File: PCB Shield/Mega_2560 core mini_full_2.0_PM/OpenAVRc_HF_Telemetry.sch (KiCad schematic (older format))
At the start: 12 parts, among them P18 Ecolage, P19 Module_TX, P20 TTL/RS232, P7 SPIX, U1 74LVC1G3157GV, U2 TLP290, U3 TLP290, U9 4050

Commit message: Delete cd4050 and move BT on board
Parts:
- removed U9: 4050, SO-16-N, symbol 4050-RESCUE-Mega_2560_core_mini_full_2.0
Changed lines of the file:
@@
 	5700 1750 5500 1750
 Connection ~ 5500 1750
-$Comp
-L 4050-RESCUE-Mega_2560_core_mini_full_2.0 U9
-U 1 1 59C530CC
-P 7300 1450
-F 0 "U9" H 7495 1565 60  0000 C CNN
-F 1 "4050" H 7490 1325 60  0000 C CNN
-F 2 "SO-16-N" H 7300 1450 60  0001 C CNN
-F 3 "" H 7300 1450 60  0001 C CNN
-	1    7300 1450
-	1    0    0    -1
-$EndComp
 Wire Notes Line
 	6250 4850 10250 4850

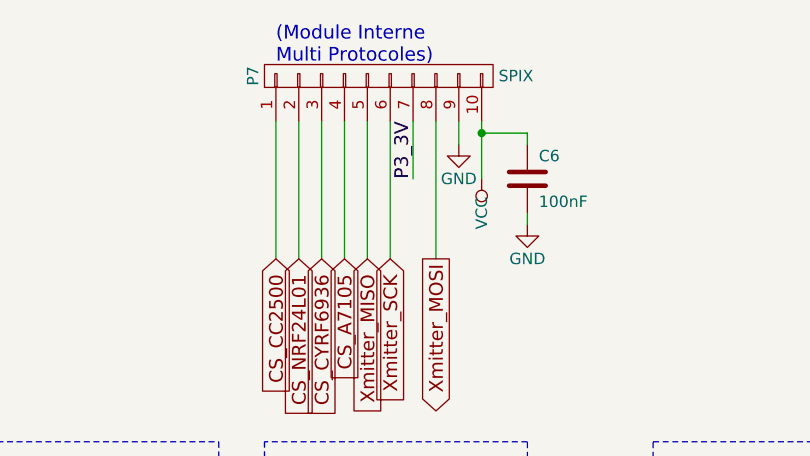
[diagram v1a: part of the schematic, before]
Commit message: Replace P3_3V signal by +3,3V (solve no connected plane on top)
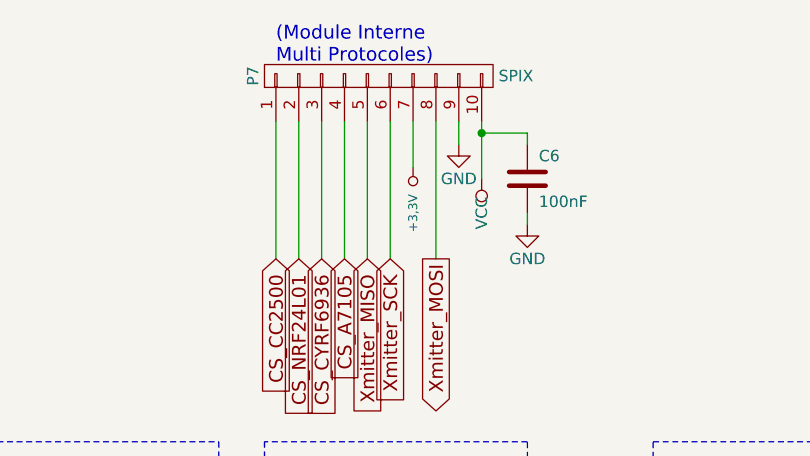
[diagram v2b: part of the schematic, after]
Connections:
- net P3_3V renamed +3.3V
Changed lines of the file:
@@
 $EndComp
 $Comp
-L GND-RESCUE-Mega_2560_core_mini_full_2.0 #PWR067
+L GND-RESCUE-Mega_2560_core_mini_full_2.0 #PWR068
 U 1 1 59C6B422
 P 1850 4600
-F 0 "#PWR067" H 1850 4350 50  0001 C CNN
+F 0 "#PWR068" H 1850 4350 50  0001 C CNN
 F 1 "GND" H 1850 4450 50  0000 C CNN
 F 2 "" H 1850 4600 50  0000 C CNN
@@
 $EndComp
 $Comp
-L +BATT #PWR068
+L +BATT #PWR069
 U 1 1 59C6B429
 P 1600 3500
-F 0 "#PWR068" H 1600 3350 50  0001 C CNN
+F 0 "#PWR069" H 1600 3350 50  0001 C CNN
 F 1 "+BATT" H 1600 3640 50  0000 C CNN
 F 2 "" H 1600 3500 50  0000 C CNN
@@
 $EndComp
 $Comp
-L GND-RESCUE-Mega_2560_core_mini_full_2.0 #PWR069
+L GND-RESCUE-Mega_2560_core_mini_full_2.0 #PWR070
 U 1 1 59C6B436
 P 5200 3900
-F 0 "#PWR069" H 5200 3650 50  0001 C CNN
+F 0 "#PWR070" H 5200 3650 50  0001 C CNN
 F 1 "GND" V 5200 3700 50  0000 C CNN
 F 2 "" H 5200 3900 50  0000 C CNN
@@
 Master_PPMout
 $Comp
-L VCC #PWR070
+L VCC #PWR071
 U 1 1 59C6B43D
 P 5300 3900
-F 0 "#PWR070" H 5300 3750 50  0001 C CNN
+F 0 "#PWR071" H 5300 3750 50  0001 C CNN
 F 1 "VCC" V 5300 4100 50  0000 C CNN
 F 2 "" H 5300 3900 50  0000 C CNN
@@
 Isolation Module TTL
 $Comp
-L +BATT #PWR071
+L +BATT #PWR072
 U 1 1 59C6B445
 P 4800 3900
-F 0 "#PWR071" H 4800 3750 50  0001 C CNN
+F 0 "#PWR072" H 4800 3750 50  0001 C CNN
 F 1 "+BATT" H 4800 4040 50  0000 C CNN
 F 2 "" H 4800 3900 50  0000 C CNN
@@
 $EndComp
 $Comp
-L GND-RESCUE-Mega_2560_core_mini_full_2.0 #PWR072
+L GND-RESCUE-Mega_2560_core_mini_full_2.0 #PWR073
 U 1 1 59C6B464
 P 9650 4500
-F 0 "#PWR072" H 9650 4250 50  0001 C CNN
+F 0 "#PWR073" H 9650 4250 50  0001 C CNN
 F 1 "GND" H 9650 4350 50  0000 C CNN
 F 2 "" H 9650 4500 50  0000 C CNN
@@
 $EndComp
 $Comp
-L GND-RESCUE-Mega_2560_core_mini_full_2.0 #PWR073
+L GND-RESCUE-Mega_2560_core_mini_full_2.0 #PWR074
 U 1 1 59C6B478
 P 3750 4400
-F 0 "#PWR073" H 3750 4150 50  0001 C CNN
+F 0 "#PWR074" H 3750 4150 50  0001 C CNN
 F 1 "GND" H 3750 4250 50  0000 C CNN
 F 2 "" H 3750 4400 50  0000 C CNN
@@
 $EndComp
 $Comp
-L VCC #PWR074
+L VCC #PWR075
 U 1 1 59C6B47E
 P 3700 3600
-F 0 "#PWR074" H 3700 3450 50  0001 C CNN
+F 0 "#PWR075" H 3700 3450 50  0001 C CNN
 F 1 "VCC" H 3700 3750 50  0000 C CNN
 F 2 "" H 3700 3600 50  0000 C CNN
@@
 $EndComp
 $Comp
-L VCC #PWR075
+L VCC #PWR076
 U 1 1 59C6B497
 P 8800 3900
-F 0 "#PWR075" H 8800 3750 50  0001 C CNN
+F 0 "#PWR076" H 8800 3750 50  0001 C CNN
 F 1 "VCC" H 8800 4050 50  0000 C CNN
 F 2 "" H 8800 3900 50  0000 C CNN
@@
 $EndComp
 $Comp
-L GND-RESCUE-Mega_2560_core_mini_full_2.0 #PWR076
+L GND-RESCUE-Mega_2560_core_mini_full_2.0 #PWR077
 U 1 1 59C6B49D
 P 7350 3900
-F 0 "#PWR076" H 7350 3650 50  0001 C CNN
+F 0 "#PWR077" H 7350 3650 50  0001 C CNN
 F 1 "GND" H 7350 3750 50  0000 C CNN
 F 2 "" H 7350 3900 50  0000 C CNN
@@
 $EndComp
 $Comp
-L GND-RESCUE-Mega_2560_core_mini_full_2.0 #PWR077
+L GND-RESCUE-Mega_2560_core_mini_full_2.0 #PWR078
 U 1 1 59C6C686
 P 5700 2150
-F 0 "#PWR077" H 5700 1900 50  0001 C CNN
+F 0 "#PWR078" H 5700 1900 50  0001 C CNN
 F 1 "GND" H 5700 2000 50  0000 C CNN
 F 2 "" H 5700 2150 50  0000 C CNN
@@
 $EndComp
 $Comp
-L GND-RESCUE-Mega_2560_core_mini_full_2.0 #PWR078
+L GND-RESCUE-Mega_2560_core_mini_full_2.0 #PWR079
 U 1 1 59C6C68C
 P 5400 1800
-F 0 "#PWR078" H 5400 1550 50  0001 C CNN
+F 0 "#PWR079" H 5400 1550 50  0001 C CNN
 F 1 "GND" H 5400 1650 50  0000 C CNN
 F 2 "" H 5400 1800 50  0000 C CNN
@@
 $EndComp
 $Comp
-L VCC #PWR079
+L VCC #PWR080
 U 1 1 59C6C694
 P 5500 1950
-F 0 "#PWR079" H 5500 1800 50  0001 C CNN
+F 0 "#PWR080" H 5500 1800 50  0001 C CNN
 F 1 "VCC" V 5500 2100 50  0000 C CNN
 F 2 "" H 5500 1950 50  0000 C CNN
@@
 	0    -1   -1   0
 $EndComp
-Text Label 5200 1950 1    60   ~ 0
-P3_3V
 Wire Wire Line
 	5100 1700 5100 2300
@@
 	4700 1700 4700 2300
 Wire Wire Line
-	5200 1700 5200 1950
+	5200 1700 5200 1900
 Wire Wire Line
 	5700 1800 5700 1750
@@
 Text GLabel 9150 3600 2    60   Input ~ 0
 Sim_control
+$Comp
+L +3,3V #PWR081
+U 1 1 59CA7757
+P 5200 1900
+F 0 "#PWR081" H 5200 1860 30  0001 C CNN
+F 1 "+3,3V" V 5200 2100 39  0000 C CNN
+F 2 "" H 5200 1900 60  0001 C CNN
+F 3 "" H 5200 1900 60  0001 C CNN
+	1    5200 1900
+	-1   0    0    1
+$EndComp
 $EndSCHEMATC

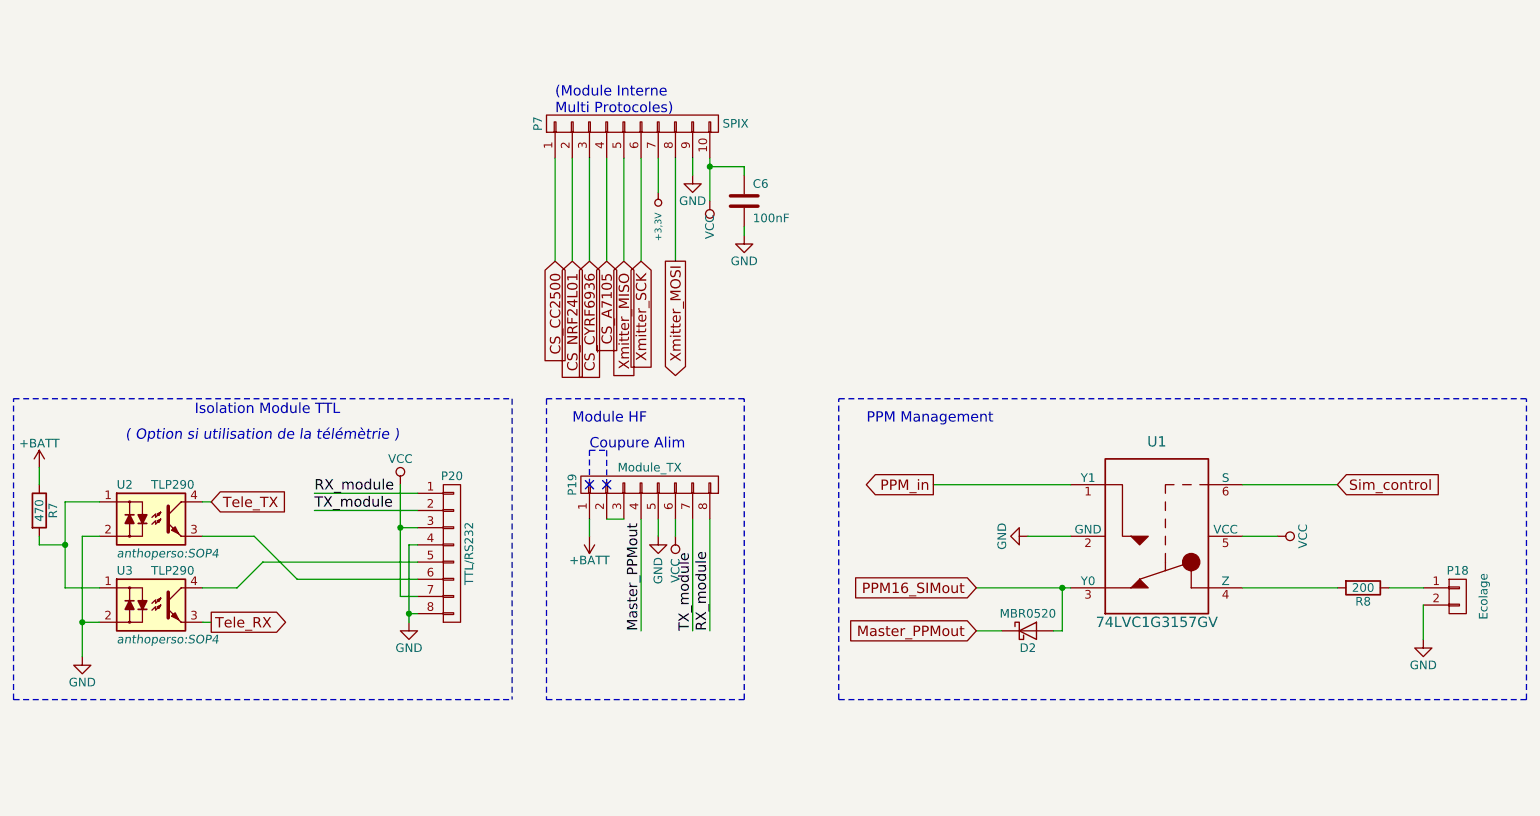
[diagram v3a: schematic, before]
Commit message: Update schematic sheets
Move Rot_2A on E7 and Rot2A on E6
Add BT_txd1 on D3 and BT_rxd1 on D2
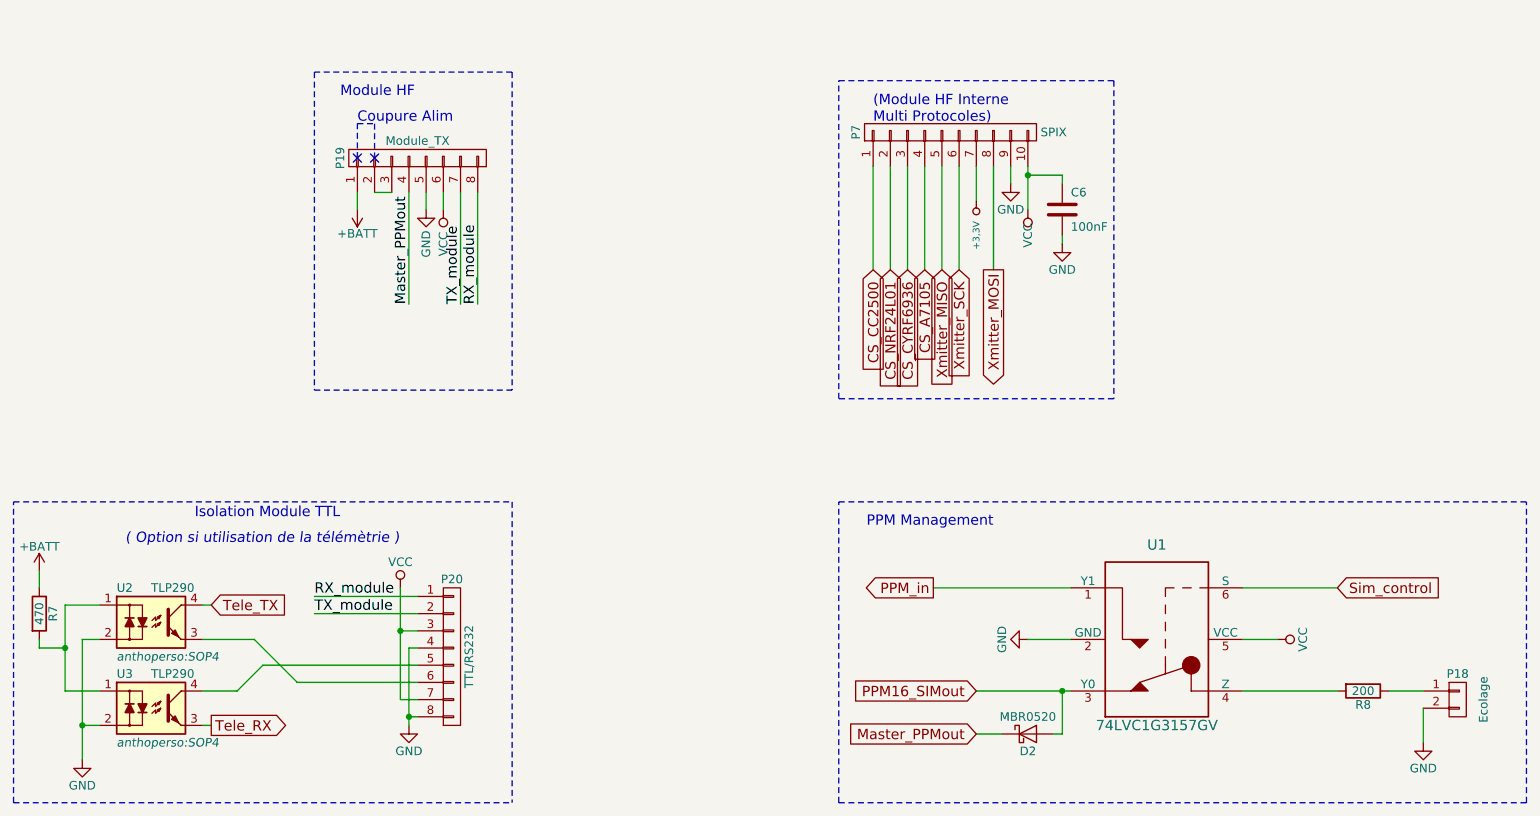
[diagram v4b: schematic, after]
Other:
- note added: "(Module HF Interne\nMulti Protocoles)"
- note removed: "(Module Interne\nMulti Protocoles)"
- moved on the sheet: C6, D2, P18, P19, P20, P7, R7, R8, U1, U2, U3

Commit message: Re-update_shield_schéma
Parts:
- removed D2: MBR0520, Diodes_SMD:D_SOD-123, symbol MBR0520
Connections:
- net PPM16_SIMout is gone; now on net Master_PPMout: U1.3 (Y0)
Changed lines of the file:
@@
 Sheet 4 7
 Title "Shield Mega2560 core Full"
-Date "2017-11-12"
+Date "2018-01-27"
 Rev "2.00"
 Comp "© Team OpenAVRc"
@@
 Text Notes 7150 3850 2    60   ~ 0
 PPM Management
-$Comp
-L MBR0520 D2
-U 1 1 59C6B455
-P 7350 5050
-F 0 "D2" H 7350 4950 50  0000 C CNN
-F 1 "MBR0520" H 7350 5150 50  0000 C CNN
-F 2 "Diodes_SMD:D_SOD-123" H 7350 4875 50  0001 C CNN
-F 3 "" H 7350 5050 50  0001 C CNN
-	1    7350 5050
-	1    0    0    -1
-$EndComp
 Text Notes 2100 3950 0    60   Italic 0
 ( Option si utilisation de la télémètrie )
@@
 	7050 4800 7600 4800
 Wire Wire Line
-	7050 5050 7200 5050
+	7050 5050 7550 5050
 Wire Wire Line
 	7550 5050 7550 4800
@@
 	3750 4950 3800 4950
 Wire Wire Line
-	7550 5050 7500 5050
-Wire Wire Line
 	3950 2000 3950 1900
